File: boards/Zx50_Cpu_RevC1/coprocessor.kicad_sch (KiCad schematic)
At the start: 17 parts, among them J7 Conn_01x06_Pin, U11 ATF1508ASx-xxJx84, U12 IS61C5128AS-25QLI, U13 SST39SF040

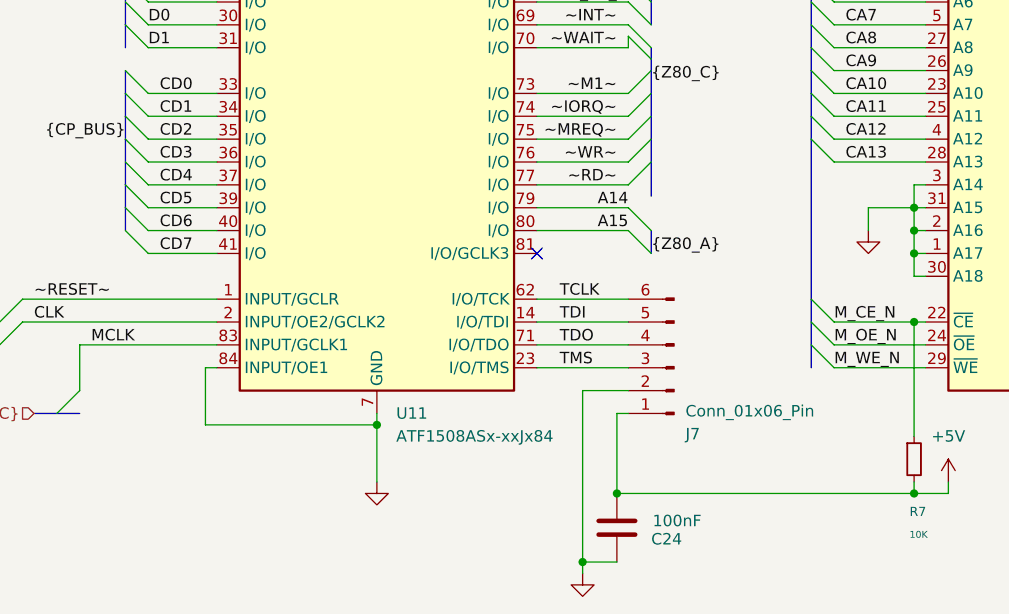
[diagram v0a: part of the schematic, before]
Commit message: init tb now runs against fpu
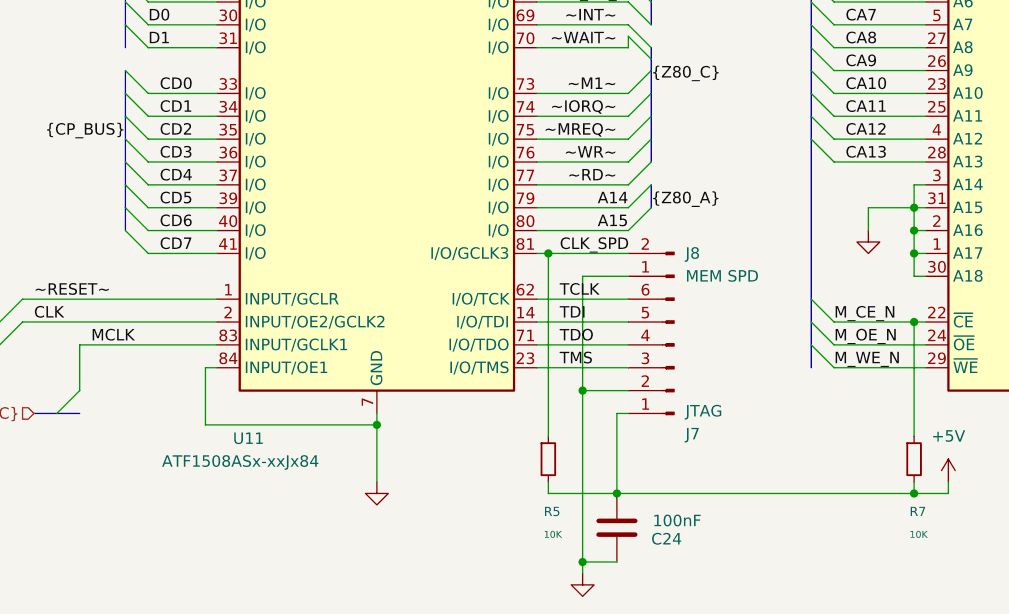
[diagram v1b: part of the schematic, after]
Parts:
- added J8: MEM SPD, Connector_PinHeader_2.54mm:PinHeader_1x02_P2.54mm_Vertical, symbol Connector:Conn_01x02_Pin
- added R5: 10K, Resistor_SMD:R_0805_2012Metric_Pad1.20x1.40mm_HandSolder, symbol Device:R_Small
- J7: value Conn_01x06_Pin -> JTAG
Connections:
- net +5V: now also R5.2
- net GND: now also J8.1 (Pin_1)
- net CLK_SPD: now reaches U11.81 (I/O/GCLK3)
- net CLK_SPD: now also J8.2 (Pin_2), R5.1
- no-connect marks 1 -> 0
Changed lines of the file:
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@@
 	)
 	(junction
+		(at 105.41 125.73)
+		(diameter 0)
+		(color 0 0 0 0)
+	)
+	(junction
 		(at 118.11 26.67)
 		(diameter 0)
@@
 	)
 	(junction
+		(at 109.22 140.97)
+		(diameter 0)
+		(color 0 0 0 0)
+	)
+	(junction
 		(at 203.2 120.65)
 		(diameter 0)
@@
 		(color 0 0 0 0)
 	)
-	(no_connect
-		(at 104.14 125.73)
-	)
 	(bus_entry
 		(at 49.53 57.15)
@@
 	)
 	(bus_entry
-		(at 116.84 123.19)
-		(size -2.54 -2.54)
+		(at 116.84 118.11)
+		(size -2.54 2.54)
 		(stroke
 			(width 0)
@@
 	)
 	(bus_entry
-		(at 116.84 125.73)
-		(size -2.54 -2.54)
+		(at 116.84 120.65)
+		(size -2.54 2.54)
 		(stroke
 			(width 0)
@@
 		)
 	)
+	(wire
+		(pts
+			(xy 109.22 128.27) (xy 109.22 140.97)
+		)
+		(stroke
+			(width 0)
+			(type default)
+		)
+	)
 	(bus
 		(pts
@@
 		)
 	)
+	(wire
+		(pts
+			(xy 105.41 151.13) (xy 105.41 152.4)
+		)
+		(stroke
+			(width 0)
+			(type default)
+		)
+	)
 	(bus
 		(pts
@@
 	(wire
 		(pts
+			(xy 105.41 152.4) (xy 113.03 152.4)
+		)
+		(stroke
+			(width 0)
+			(type default)
+		)
+	)
+	(wire
+		(pts
 			(xy 86.36 39.37) (xy 86.36 36.83)
 		)
@@
 		)
 	)
+	(wire
+		(pts
+			(xy 105.41 125.73) (xy 105.41 146.05)
+		)
+		(stroke
+			(width 0)
+			(type default)
+		)
+	)
 	(bus
 		(pts
@@
 		)
 	)
-	(bus
-		(pts
-			(xy 116.84 115.57) (xy 116.84 119.38)
-		)
-		(stroke
-			(width 0)
-			(type default)
-		)
-	)
 	(wire
 		(pts
@@
 	(wire
 		(pts
+			(xy 105.41 125.73) (xy 114.3 125.73)
+		)
+		(stroke
+			(width 0)
+			(type default)
+		)
+	)
+	(wire
+		(pts
 			(xy 203.2 123.19) (xy 205.74 123.19)
 		)
@@
 		)
 	)
+	(wire
+		(pts
+			(xy 114.3 128.27) (xy 109.22 128.27)
+		)
+		(stroke
+			(width 0)
+			(type default)
+		)
+	)
 	(bus
 		(pts
@@
 		)
 	)
+	(wire
+		(pts
+			(xy 104.14 125.73) (xy 105.41 125.73)
+		)
+		(stroke
+			(width 0)
+			(type default)
+		)
+	)
 	(bus
 		(pts
@@
 	(bus
 		(pts
-			(xy 116.84 123.19) (xy 116.84 125.73)
+			(xy 116.84 118.11) (xy 116.84 120.65)
 		)
 		(stroke
@@
 	)
 	(label "{Z80_A}"
-		(at 116.84 125.73 0)
+		(at 116.84 120.65 0)
 		(effects
 			(font
@@
 		)
 	)
+	(label "CLK_SPD"
+		(at 106.68 125.73 0)
+		(effects
+			(font
+				(size 1.27 1.27)
+			)
+			(justify left bottom)
+		)
+	)
 	(label "CA0"
 		(at 114.3 72.39 180)
@@
 		(on_board yes)
 		(dnp no)
-		(fields_autoplaced yes)
 		(property "Reference" "U11"
-			(at 88.5033 143.51 0)
+			(at 70.358 146.304 0)
 			(effects
 				(font
@@
 		)
 		(property "Value" "ATF1508ASx-xxJx84"
-			(at 88.5033 146.05 0)
+			(at 62.484 148.844 0)
 			(effects
 				(font
@@
 	)
 	(symbol
+		(lib_id "Device:R_Small")
+		(at 105.41 148.59 0)
+		(unit 1)
+		(exclude_from_sim no)
+		(in_bom yes)
+		(on_board yes)
+		(dnp no)
+		(property "Reference" "R5"
+			(at 104.902 154.432 0)
+			(effects
+				(font
+					(size 1.016 1.016)
+				)
+				(justify left)
+			)
+		)
+		(property "Value" "10K"
+			(at 104.902 156.972 0)
+			(effects
+				(font
+					(size 0.762 0.762)
+				)
+				(justify left)
+			)
+		)
+		(property "Footprint" "Resistor_SMD:R_0805_2012Metric_Pad1.20x1.40mm_HandSolder"
+			(at 105.41 148.59 0)
+			(effects
+				(font
+					(size 1.27 1.27)
+				)
+				(hide yes)
+			)
+		)
+		(property "Datasheet" "~"
+			(at 105.41 148.59 0)
+			(effects
+				(font
+					(size 1.27 1.27)
+				)
+				(hide yes)
+			)
+		)
+		(property "Description" "Resistor, small symbol"
+			(at 105.41 148.59 0)
+			(effects
+				(font
+					(size 1.27 1.27)
+				)
+				(hide yes)
+			)
+		)
+		(pin "2"
+		)
+		(pin "1"
+		)
+		(instances
+			(project "Zx50_Cpu_RevC1"
+				(path "/d27e6793-29e8-4553-aae0-c58a11de5d25/b98b1677-4c21-433e-bc3e-64f5e8297f28"
+					(reference "R5")
+					(unit 1)
+				)
+			)
+		)
+	)
+	(symbol
 		(lib_id "Connector:Conn_01x06_Pin")
 		(at 119.38 138.43 180)
@@
 			)
 		)
-		(property "Value" "Conn_01x06_Pin"
+		(property "Value" "JTAG"
 			(at 120.65 143.256 0)
 			(effects
@@
 					(unit 1)
 				)
+			)
+		)
+	)
+	(symbol
+		(lib_id "Connector:Conn_01x02_Pin")
+		(at 119.38 128.27 180)
+		(unit 1)
+		(exclude_from_sim no)
+		(in_bom yes)
+		(on_board yes)
+		(dnp no)
+		(property "Reference" "J8"
+			(at 120.65 125.7299 0)
+			(effects
+				(font
+					(size 1.27 1.27)
+				)
+				(justify right)
+			)
+		)
+		(property "Value" "MEM SPD"
+			(at 120.65 128.2699 0)
+			(effects
+				(font
+					(size 1.27 1.27)
+				)
+				(justify right)
+			)
+		)
+		(property "Footprint" "Connector_PinHeader_2.54mm:PinHeader_1x02_P2.54mm_Vertical"
+			(at 119.38 128.27 0)
+			(effects
+				(font
+					(size 1.27 1.27)
+				)
+				(hide yes)
+			)
+		)
+		(property "Datasheet" "~"
+			(at 119.38 128.27 0)
+			(effects
+				(font
+					(size 1.27 1.27)
+				)
+				(hide yes)
+			)
+		)
+		(property "Description" "Generic connector, single row, 01x02, script generated"
+			(at 119.38 128.27 0)
+			(effects
+				(font
+					(size 1.27 1.27)
+				)
+				(hide yes)
+			)
+		)
+		(pin "1"
+		)
+		(pin "2"
+		)
+		(instances
+			(project ""
+				(path "/d27e6793-29e8-4553-aae0-c58a11de5d25/b98b1677-4c21-433e-bc3e-64f5e8297f28"
+					(reference "J8")
+					(unit 1)
+				)
